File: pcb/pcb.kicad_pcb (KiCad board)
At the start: 2 copper layers, 109 x 54 mm, 60 parts, among them J1 MALE, J10 TC2030_NL, J101 MALE, J102 FEMALE, J103 MALE, J104 FEMALE, J105 MALE, J106 FEMALE, J107 MALE, J108 FEMALE, J11 STANDOFF, J111 STANDOFF, J112 STANDOFF, J113 STANDOFF, J114 STANDOFF, J12 STANDOFF, J13 STANDOFF, J14 STANDOFF, J2 FEMALE, J3 MALE, J4 FEMALE, J5 MALE, J6 FEMALE, J7 MALE, J8 FEMALE, J9 DTR, Q1 2N3904, SW1 ACTION, SW2 ACTION, SW3 ACTION, SW4 ACTION, U3 ATmega328P-MU, Y1 YSX321SL

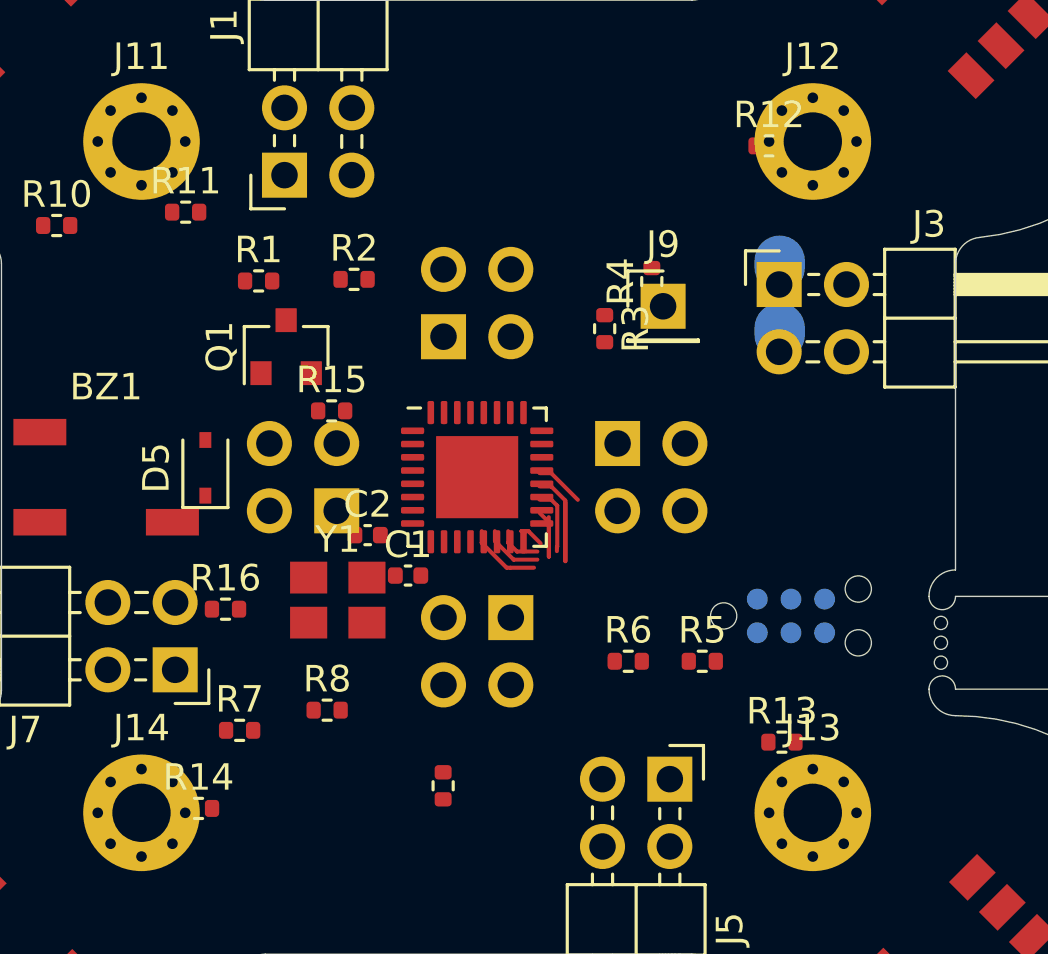
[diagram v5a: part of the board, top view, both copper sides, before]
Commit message: Round power for bottom
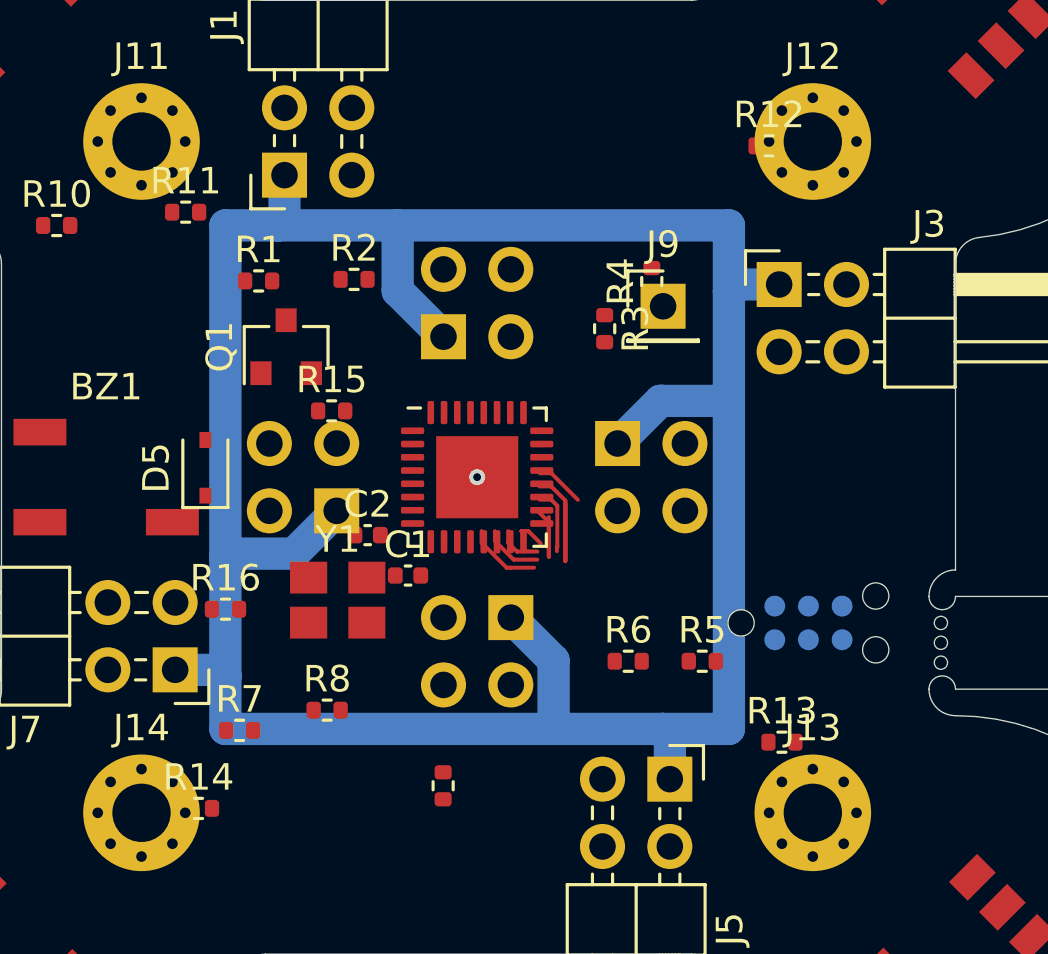
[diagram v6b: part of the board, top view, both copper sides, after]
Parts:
- moved J10 0.71 mm to (133.5, 110.5)
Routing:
- net +5VB: track 0.25 -> 103.7 mm
- net GNDB: track 2.11 -> 1.86 mm, vias 0 -> 1
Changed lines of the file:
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@@
     (thickness 1)
     (drawings 112)
-    (tracks 141)
+    (tracks 171)
     (zones 0)
     (modules 60)
@@
   (layers
     (0 F.Cu signal)
-    (31 B.Cu signal hide)
+    (31 B.Cu signal)
     (32 B.Adhes user hide)
     (33 F.Adhes user hide)
@@
     (37 F.SilkS user hide)
     (38 B.Mask user hide)
-    (39 F.Mask user)
+    (39 F.Mask user hide)
     (40 Dwgs.User user hide)
     (41 Cmts.User user hide)
@@
   )
   (setup
-    (last_trace_width 0.1524)
+    (last_trace_width 1.2192)
     (user_trace_width 0.1524)
     (user_trace_width 1.2192)
@@
   )
   (module Connector:Tag-Connect_TC2030-IDC-NL_2x03_P1.27mm_Vertical (layer B.Cu)
-    (at 132.842 110.236)
+    (at 133.5 110.5)
     (descr "Tag-Connect programming header; http://www.tag-connect.com/Materials/TC2030-IDC-NL.pdf")
     (tags "tag connect programming header pogo pins")
@@
   (gr_circle (center 134.936 97.73) (end 135.936 97.73) (layer Dwgs.User) (width 0.05))
   (gr_circle (center 133.666 92.333999) (end 136.166 92.333999) (layer Dwgs.User) (width 0.05))
+  (via (at 121 105) (size 0.6) (drill 0.3) (layers F.Cu B.Cu) (net 50))
   (segment (start 190.552854 122.204505) (end 192.174174 123.825826) (width 0.1524) (layer F.Cu) (net 1))
   (segment (start 157.204505 83.552854) (end 159.325825 85.674175) (width 0.1524) (layer F.Cu) (net 1))
@@
   (segment (start 123.3575 105.35) (end 123.795 105.35) (width 0.1524) (layer F.Cu) (net 41))
   (segment (start 124.32842 108.17158) (end 124.32842 105.952354) (width 0.1524) (layer F.Cu) (net 41))
-  (segment (start 132.416 97.088) (end 132.416 96.834) (width 1.905) (layer B.Cu) (net 49))
+  (segment (start 130.77 97.73) (end 130.5 98) (width 1.2192) (layer B.Cu) (net 49))
+  (segment (start 132.396 97.73) (end 130.77 97.73) (width 1.2192) (layer B.Cu) (net 49))
+  (segment (start 130.5 98) (end 130.5 95.5) (width 1.2192) (layer B.Cu) (net 49))
+  (segment (start 130.382001 102.117999) (end 130.5 102) (width 1.2192) (layer B.Cu) (net 49))
+  (segment (start 127.912001 102.117999) (end 130.382001 102.117999) (width 1.2192) (layer B.Cu) (net 49))
+  (segment (start 130.5 102) (end 130.5 98) (width 1.2192) (layer B.Cu) (net 49))
+  (segment (start 126.3 103.73) (end 127.912001 102.117999) (width 1.2192) (layer B.Cu) (net 49))
+  (segment (start 130.5 114.5) (end 130.5 102) (width 1.2192) (layer B.Cu) (net 49))
+  (segment (start 128.27 114.77) (end 128 114.5) (width 1.2192) (layer B.Cu) (net 49))
+  (segment (start 128.27 116.396) (end 128.27 114.77) (width 1.2192) (layer B.Cu) (net 49))
+  (segment (start 128 114.5) (end 130.5 114.5) (width 1.2192) (layer B.Cu) (net 49))
+  (segment (start 123.882001 114.382001) (end 124 114.5) (width 1.2192) (layer B.Cu) (net 49))
+  (segment (start 123.882001 111.912001) (end 123.882001 114.382001) (width 1.2192) (layer B.Cu) (net 49))
+  (segment (start 122.27 110.3) (end 123.882001 111.912001) (width 1.2192) (layer B.Cu) (net 49))
+  (segment (start 124 114.5) (end 128 114.5) (width 1.2192) (layer B.Cu) (net 49))
+  (segment (start 111.5 114.5) (end 124 114.5) (width 1.2192) (layer B.Cu) (net 49))
+  (segment (start 111.617999 107.882001) (end 111.5 108) (width 1.2192) (layer B.Cu) (net 49))
+  (segment (start 115.7 106.27) (end 114.087999 107.882001) (width 1.2192) (layer B.Cu) (net 49))
+  (segment (start 114.087999 107.882001) (end 111.617999 107.882001) (width 1.2192) (layer B.Cu) (net 49))
+  (segment (start 111.5 95.5) (end 111.5 108) (width 1.2192) (layer B.Cu) (net 49))
+  (segment (start 118 97.97) (end 118 95.5) (width 1.2192) (layer B.Cu) (net 49))
+  (segment (start 119.73 99.7) (end 118 97.97) (width 1.2192) (layer B.Cu) (net 49))
+  (segment (start 118 95.5) (end 130.5 95.5) (width 1.2192) (layer B.Cu) (net 49))
+  (segment (start 113.73 95.27) (end 113.5 95.5) (width 1.2192) (layer B.Cu) (net 49))
+  (segment (start 113.73 93.604) (end 113.73 95.27) (width 1.2192) (layer B.Cu) (net 49))
+  (segment (start 113.5 95.5) (end 118 95.5) (width 1.2192) (layer B.Cu) (net 49))
+  (segment (start 111.5 95.5) (end 113.5 95.5) (width 1.2192) (layer B.Cu) (net 49))
+  (segment (start 111.27 112.27) (end 111.5 112.5) (width 1.2192) (layer B.Cu) (net 49))
+  (segment (start 109.604 112.27) (end 111.27 112.27) (width 1.2192) (layer B.Cu) (net 49))
+  (segment (start 111.5 112.5) (end 111.5 114.5) (width 1.2192) (layer B.Cu) (net 49))
+  (segment (start 111.5 108) (end 111.5 112.5) (width 1.2192) (layer B.Cu) (net 49))
   (segment (start 123.795 104.85) (end 124.8 105.855) (width 0.1524) (layer F.Cu) (net 50))
   (segment (start 123.3575 104.85) (end 123.795 104.85) (width 0.1524) (layer F.Cu) (net 50))
-  (segment (start 132.416 99.628) (end 132.416 99.374) (width 1.905) (layer B.Cu) (net 50))
   (segment (start 178.77033 97.16) (end 177.27 97.16) (width 0.1524) (layer B.Cu) (net 53))
   (segment (start 182.191399 93.738931) (end 178.77033 97.16) (width 0.1524) (layer B.Cu) (net 53))

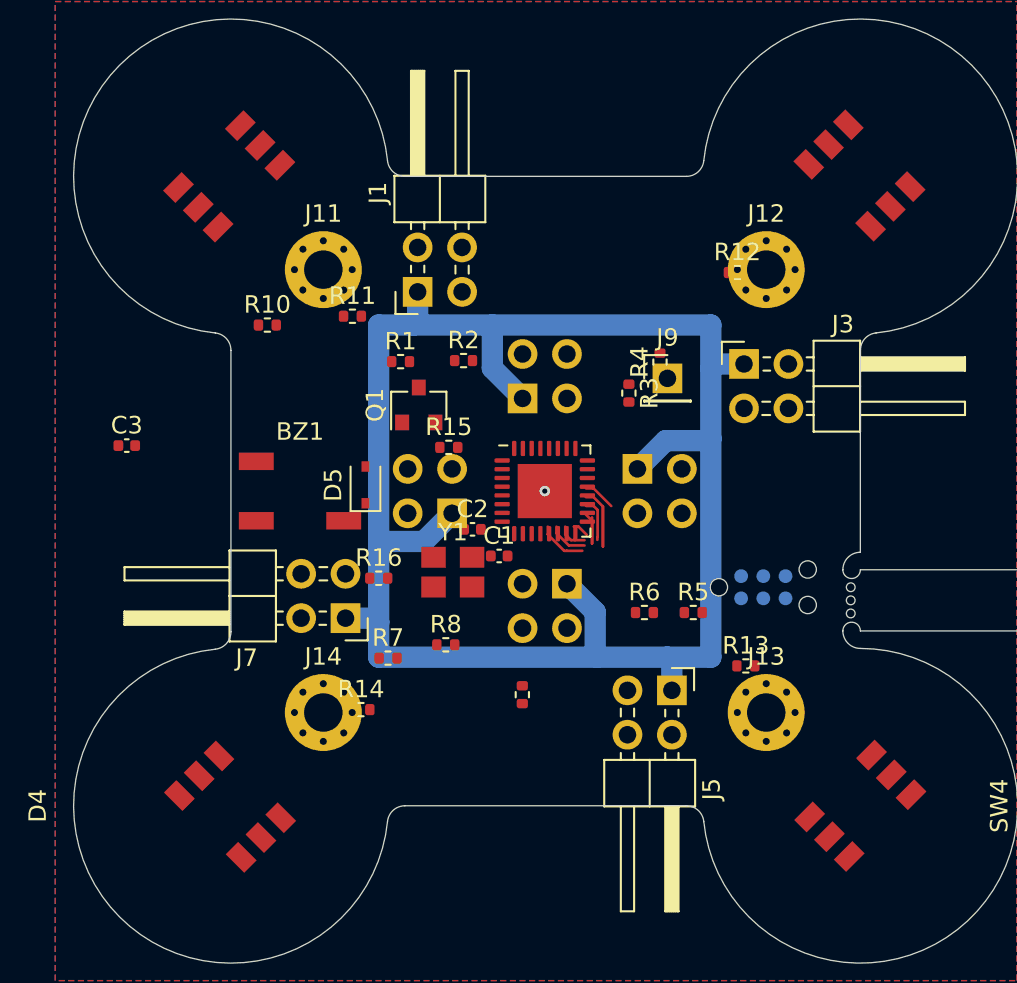
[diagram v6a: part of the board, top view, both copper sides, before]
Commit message: Route top board (but DRC errors)
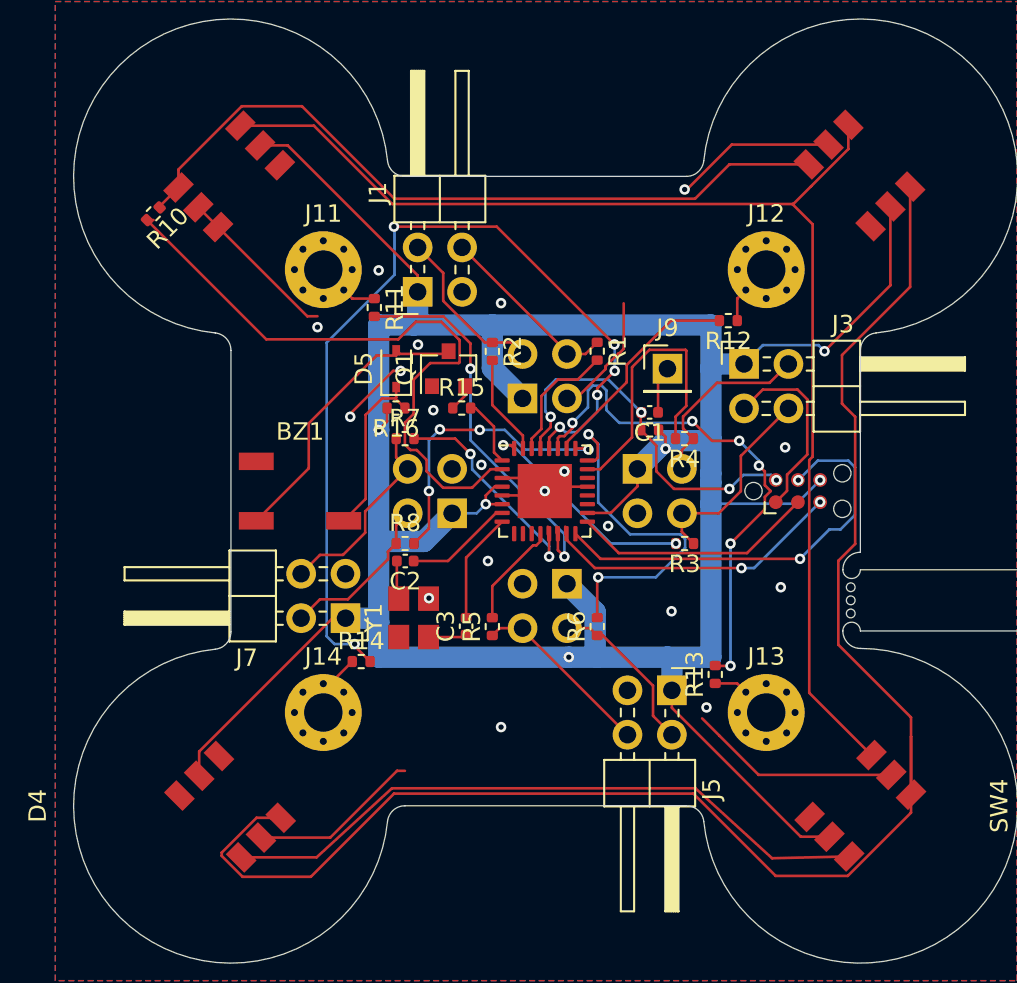
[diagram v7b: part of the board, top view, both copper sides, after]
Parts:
- J10: moved to F.Cu
- moved C3 22.0 mm to (116.5, 112.7), turned to 90 degrees
- moved R9 16.8 mm to (127.0, 101.5), turned to 180 degrees
- moved R7 12.6 mm to (113.0, 102.0)
- moved C1 11.9 mm to (127.0, 100.5), turned to 180 degrees
- moved R5 11.5 mm to (118.0, 112.8), turned to 90 degrees
- moved R1 11.3 mm to (124.0, 97.0), turned to 270 degrees
- moved R16 9.78 mm to (112.5, 100.2), turned to 180 degrees
- moved R3 9.17 mm to (129.0, 108.0), turned to 180 degrees
- moved R10 9.11 mm to (98.6, 89.1), turned to 225 degrees
- moved D5 6.88 mm to (112.5, 98.0)
- moved R8 6.24 mm to (113.0, 108.0)
- moved J10 5.85 mm to (135.5, 105.0)
- moved R4 4.60 mm to (129.0, 102.0), turned to 180 degrees
- moved C2 4.25 mm to (113.0, 109.0), turned to 180 degrees
- moved Y1 3.44 mm to (113.5, 112.2), turned to 90 degrees
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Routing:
- net Net-(D2-Pad3): track 0.00 -> 92.9 mm
- net Net-(D1-Pad3): track 0.00 -> 72.9 mm
- net +5VB: track 103.7 -> 176.1 mm, vias 0 -> 6
- net GNDB: track 1.86 -> 70.6 mm, vias 1 -> 19
- net Net-(R14-Pad2): track 0.00 -> 52.1 mm, vias 0 -> 6
- net /Bottom/DIN: track 0.00 -> 43.2 mm
- net Net-(D3-Pad3): track 0.00 -> 37.9 mm
- net Net-(R10-Pad2): track 0.00 -> 37.6 mm
- net Net-(R13-Pad2): track 0.00 -> 30.5 mm, vias 0 -> 6
- net /Bottom/MISO: track 1.06 -> 24.2 mm, vias 0 -> 2
- net /Bottom/~RST: track 0.00 -> 21.8 mm, vias 0 -> 4
- net Net-(R6-Pad2): track 0.00 -> 20.7 mm, vias 0 -> 2
- net Net-(R11-Pad2): track 2.26 -> 22.4 mm, vias 0 -> 2
- net Net-(BZ1-Pad2): track 0.00 -> 16.9 mm
- net Net-(R8-Pad2): track 0.00 -> 16.9 mm, vias 0 -> 4
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
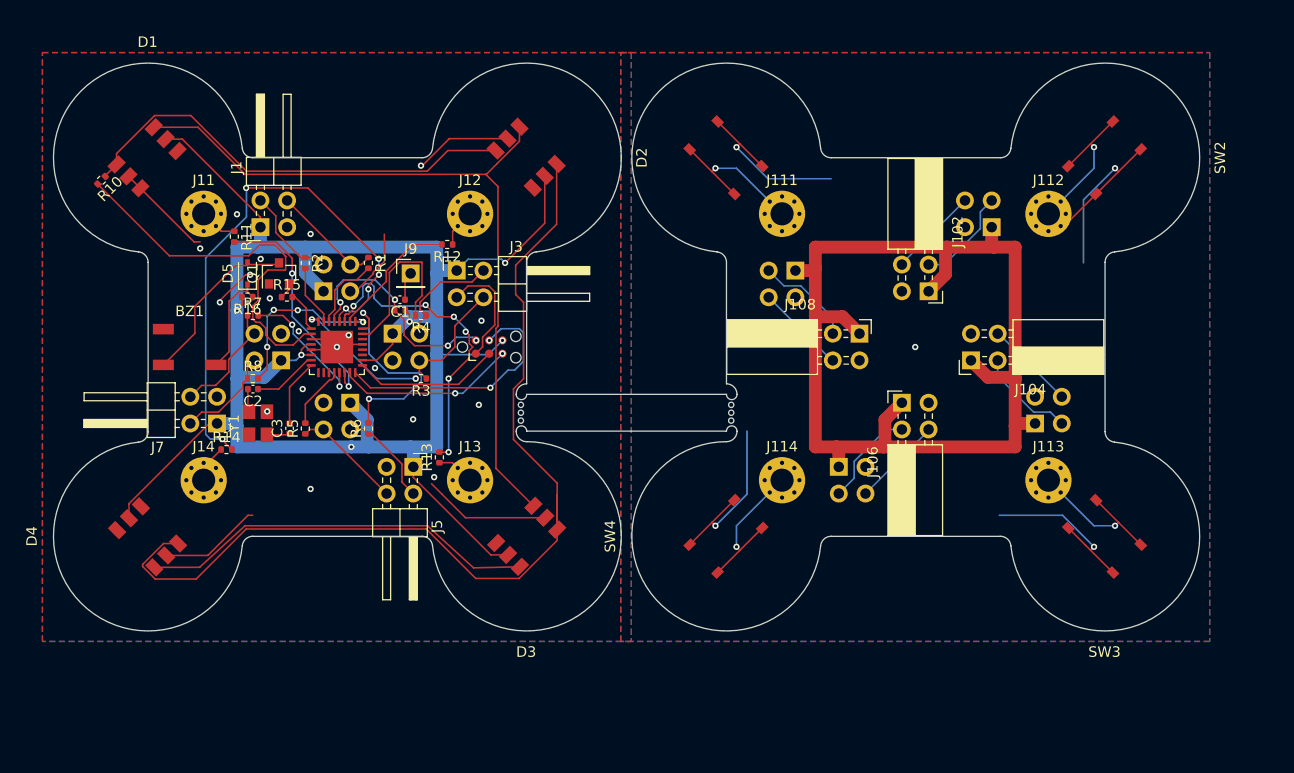
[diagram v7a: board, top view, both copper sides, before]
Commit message: Fix: overlapping fill zones
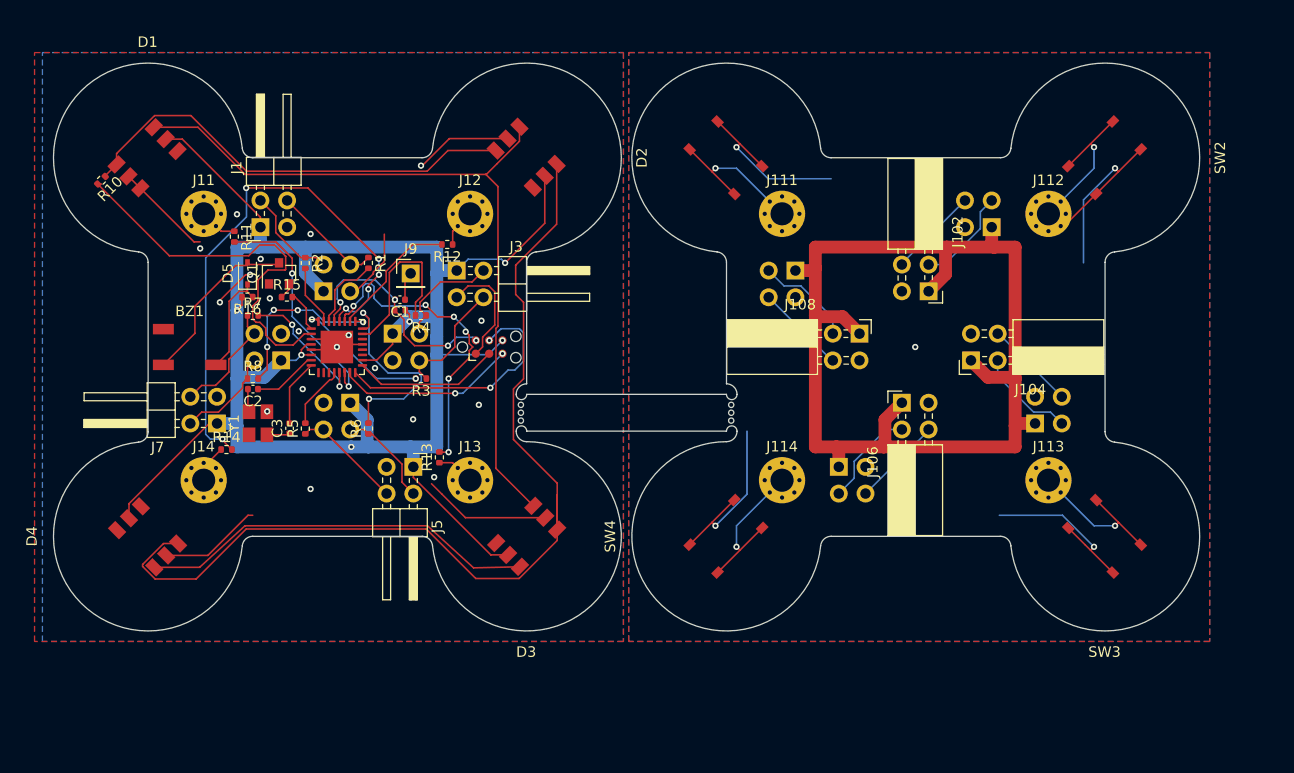
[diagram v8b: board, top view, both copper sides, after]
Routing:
- net Net-(BZ1-Pad2): track 16.9 -> 21.0 mm, vias 0 -> 2
- net GNDB: track 70.6 -> 66.5 mm, vias 19 -> 16
- net Net-(J11-Pad1): vias 0 -> 1
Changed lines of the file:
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@@
   )
   (layers
-    (0 F.Cu signal)
+    (0 F.Cu signal hide)
     (31 B.Cu signal)
     (32 B.Adhes user hide)
@@
   (segment (start 137.232233 85.182233) (end 131.696478 85.182233) (width 0.1524) (layer F.Cu) (net 50))
   (via (at 118.5 94.25) (size 0.6) (drill 0.3) (layers F.Cu B.Cu) (net 50))
-  (via (at 111.5 92.375) (size 0.6) (drill 0.3) (layers F.Cu B.Cu) (net 50))
+  (via (at 111.5 92.375) (size 0.6) (drill 0.3) (layers F.Cu B.Cu) (net 67))
   (via (at 117.375 103.5) (size 0.6) (drill 0.3) (layers F.Cu B.Cu) (net 50))
   (via (at 128.25 111.875) (size 0.6) (drill 0.3) (layers F.Cu B.Cu) (net 50))
@@
   (via (at 108 95.625) (size 0.6) (drill 0.3) (layers F.Cu B.Cu) (net 50))
   (via (at 113.75 96.625) (size 0.6) (drill 0.3) (layers F.Cu B.Cu) (net 50))
-  (via (at 112.75 98.125) (size 0.6) (drill 0.3) (layers F.Cu B.Cu) (net 50))
-  (via (at 109.875 100.75) (size 0.6) (drill 0.3) (layers F.Cu B.Cu) (net 50))
-  (segment (start 109.875 100.575736) (end 109.875 100.75) (width 0.1524) (layer F.Cu) (net 50))
-  (segment (start 112.325736 98.125) (end 109.875 100.575736) (width 0.1524) (layer F.Cu) (net 50))
-  (segment (start 112.75 98.125) (end 112.325736 98.125) (width 0.1524) (layer F.Cu) (net 50))
+  (via (at 112.75 98.125) (size 0.6) (drill 0.3) (layers F.Cu B.Cu) (net 66))
+  (via (at 109.875 100.75) (size 0.6) (drill 0.3) (layers F.Cu B.Cu) (net 66))
+  (segment (start 109.875 100.575736) (end 109.875 100.75) (width 0.1524) (layer F.Cu) (net 66))
+  (segment (start 112.325736 98.125) (end 109.875 100.575736) (width 0.1524) (layer F.Cu) (net 66))
+  (segment (start 112.75 98.125) (end 112.325736 98.125) (width 0.1524) (layer F.Cu) (net 66))
   (via (at 130.25 117.375) (size 0.6) (drill 0.3) (layers F.Cu B.Cu) (net 50))
   (via (at 118.5 118.5) (size 0.6) (drill 0.3) (layers F.Cu B.Cu) (net 50))
@@
     (polygon
       (pts
-        (xy 204 133) (xy 148 133) (xy 148 77) (xy 204 77)
+        (xy 204 133) (xy 148.75 133) (xy 148.75 77) (xy 204 77)
       )
     )
@@
     (polygon
       (pts
-        (xy 149 133) (xy 93 133) (xy 93 77) (xy 149 77)
+        (xy 148.25 133) (xy 93 133) (xy 93 77) (xy 148.25 77)
       )
     )
@@
     (polygon
       (pts
-        (xy 149 133) (xy 93 133) (xy 93 77) (xy 149 77)
+        (xy 148.25 133) (xy 92.25 133) (xy 92.25 77) (xy 148.25 77)
       )
     )
@@
     (polygon
       (pts
-        (xy 204 133) (xy 148 133) (xy 148 77) (xy 204 77)
+        (xy 204 133) (xy 148.75 133) (xy 148.75 77) (xy 204 77)
       )
     )
